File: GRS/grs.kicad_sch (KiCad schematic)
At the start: 7 parts, among them Q1 TIP120, U1 Teensy4.1, U2 TSR_1-2450, U3 BME280

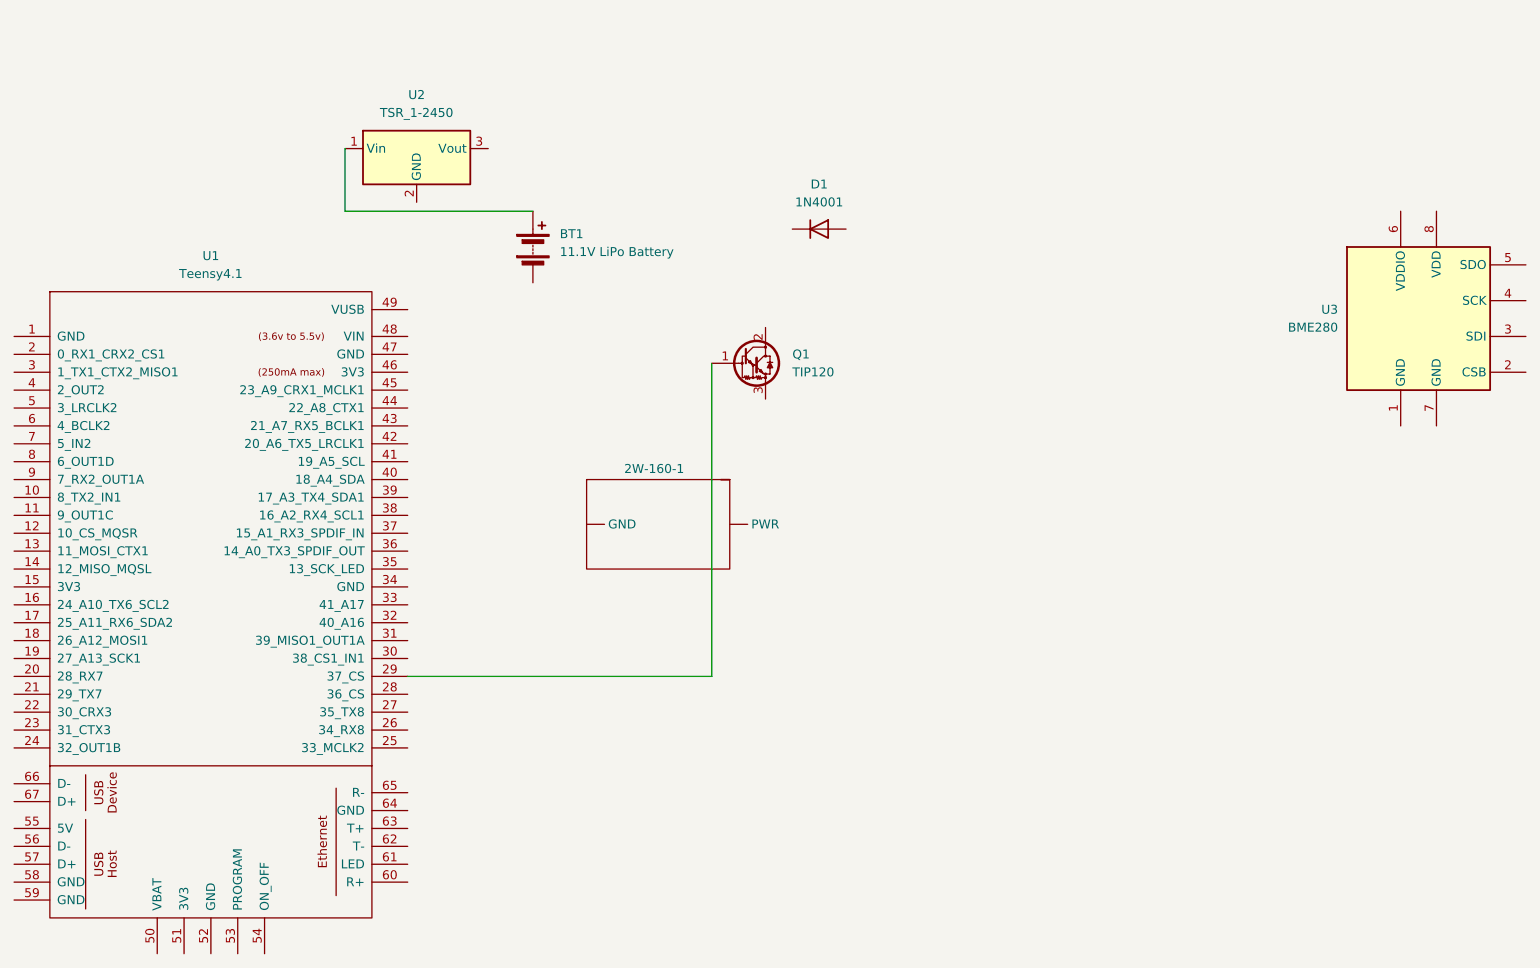
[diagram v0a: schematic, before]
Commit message: cleaned up valve symbol and partially completed wiring for valve control, teensy needs to be powered and connected to circuit
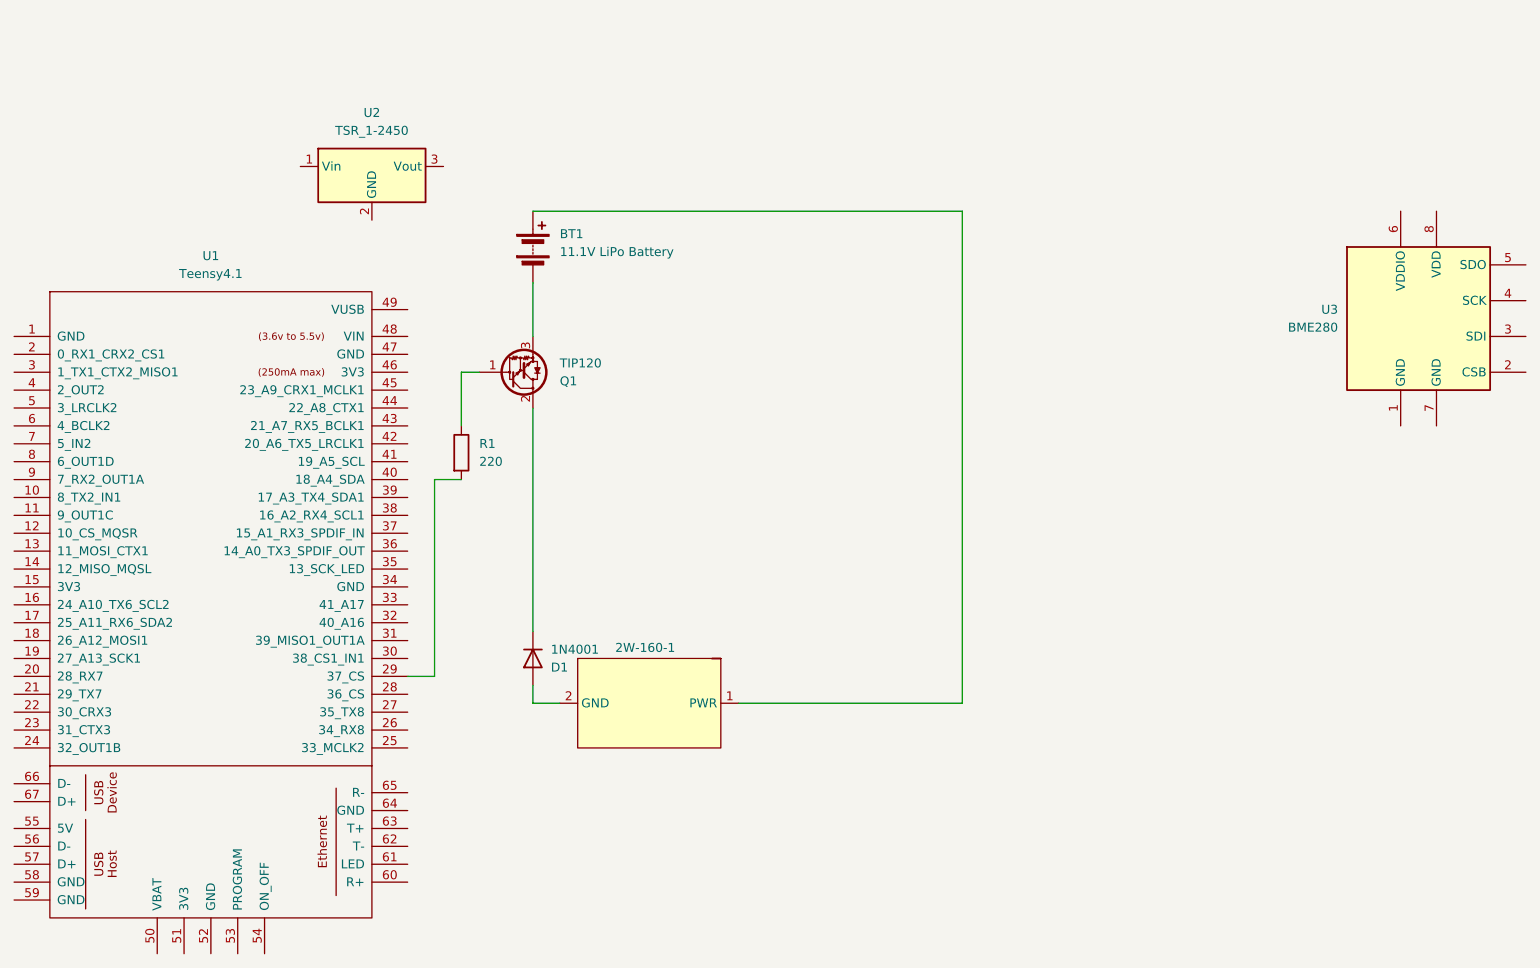
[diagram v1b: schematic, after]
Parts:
- added R1: 220, symbol Device:R
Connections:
- net at U1.29 (37_CS): now also R1.2; no longer Q1.1 (B)
- net at D1.1 (K): now also Q1.2 (C)
- net at D1.2 (A): now also 2W-160-1.2 (GND)
- net at BT1.1 (+): now also 2W-160-1.1 (PWR); no longer U2.1 (Vin)
- net at BT1.2 (-): now also Q1.3 (E)
- new net: Q1.1 (B), R1.1
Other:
- moved on the sheet: D1, Q1, U2

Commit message: prototyped summing circuit and SiPM
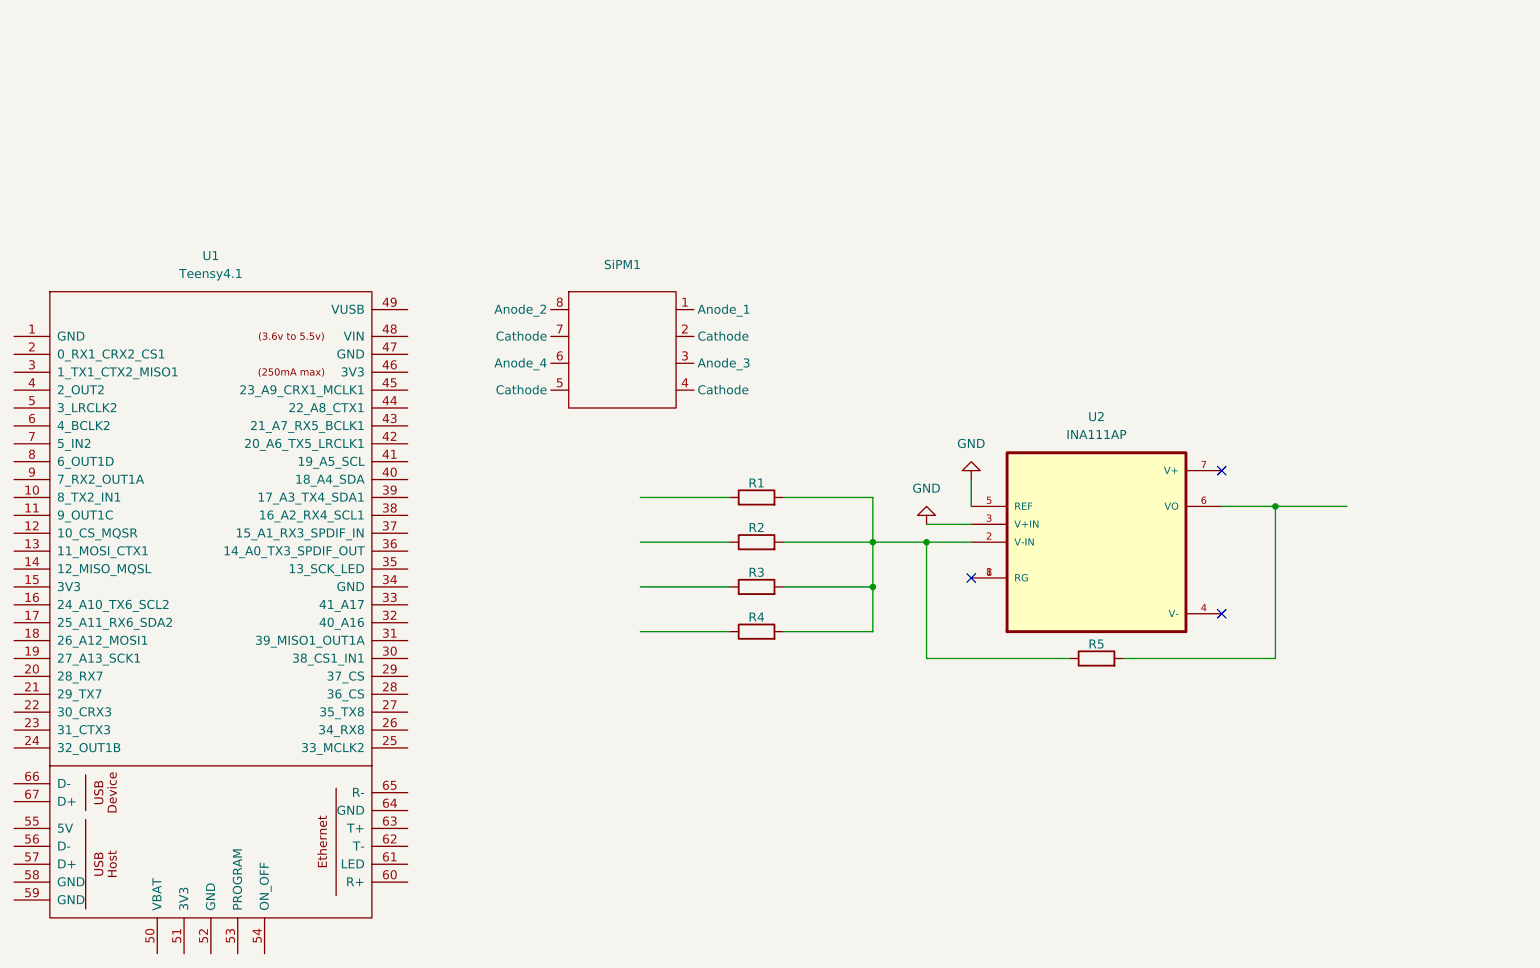
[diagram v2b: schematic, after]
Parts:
- removed 2W-160-1: ~, symbol GRS_Valve:2W-160-15
- removed BT1: 11.1V LiPo Battery, symbol Device:Battery
- removed D1: 1N4001, Diode_THT:D_DO-41_SOD81_P10.16mm_Horizontal, symbol Diode:1N4001
- removed Q1: TIP120, Package_TO_SOT_THT:TO-220-3_Vertical, symbol Transistor_BJT:TIP120
- removed U2: TSR_1-2450, Converter_DCDC:Converter_DCDC_TRACO_TSR-1_THT, symbol Regulator_Switching:TSR_1-2450
- removed U3: BME280, Package_LGA:Bosch_LGA-8_2.5x2.5mm_P0.65mm_ClockwisePinNumbering, symbol Sensor:BME280
- added R2, R3, R4, R5: R, symbol Device:R
- added SiPM1: ~, symbol HAB:SiPM
- added U2: INA111AP, INA111AP:DIP794W45P254L959H508Q8, symbol INA111AP:INA111AP
- R1: value 220 -> R
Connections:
- net at U1.29 (37_CS): no longer R1.2
- new net: R1.2, R2.2, R3.2, R4.2, R5.1, U2.2 (V-IN)
- new net: U2.1 (RG), U2.8 (RG)
- new net: R5.2, U2.6 (VO)
- new net GND: U2.3 (V+IN), U2.5 (REF)
- no-connect marks 0 -> 3

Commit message: made peak detector footprint
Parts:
- added PKD01FP1: ~, symbol New_Library:PKD01FP
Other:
- note added: "GRS Schematic"
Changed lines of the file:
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@@
+		)
+	)
+	(text "GRS Schematic"
+		(exclude_from_sim no)
+		(at 195.072 189.738 0)
+		(effects
+			(font
+				(size 1.27 1.27)
+			)
 		)
 	)
@@
 					(unit 1)
 				)
+			)
+		)
+	)
+	(symbol
+		(lib_id "New_Library:PKD01FP")
+		(at 107.95 63.5 0)
+		(unit 1)
+		(exclude_from_sim no)
+		(in_bom yes)
+		(on_board yes)
+		(dnp no)
+		(fields_autoplaced yes)
+		(property "Reference" "PKD01FP1"
+			(at 107.95 60.96 0)
+			(effects
+				(font
+					(size 1.27 1.27)
+				)
+			)
+		)
+		(property "Value" "~"
+			(at 107.95 63.5 0)
+			(effects
+				(font
+					(size 1.27 1.27)
+				)
+			)
+		)
+		(property "Footprint" ""
+			(at 107.95 63.5 0)
+			(effects
+				(font
+					(size 1.27 1.27)
+				)
+				(hide yes)
+			)
+		)
+		(property "Datasheet" ""
+			(at 107.95 63.5 0)
+			(effects
+				(font
+					(size 1.27 1.27)
+				)
+				(hide yes)
+			)
+		)
+		(property "Description" ""
+			(at 107.95 63.5 0)
+			(effects
+				(font
+					(size 1.27 1.27)
+				)
+				(hide yes)
+			)
+		)
+		(pin "3"
+		)
+		(pin "5"
+		)
+		(pin "6"
+		)
+		(pin "8"
+		)
+		(pin "4"
+		)
+		(pin "7"
+		)
+		(pin "13"
+		)
+		(pin "9"
+		)
+		(pin "11"
+		)
+		(pin "1"
+		)
+		(pin "12"
+		)
+		(pin "2"
+		)
+		(pin "10"
+		)
+		(pin "14"
+		)
+		(instances
+			(project ""
+				(path "/da212a0e-0325-4de6-8fc7-5f35040c02c9"
+					(reference "PKD01FP1")
+					(unit 1)
+				)
